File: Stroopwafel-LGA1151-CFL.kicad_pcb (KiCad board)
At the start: 2 copper layers, 2 parts

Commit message: replaced PCH symbol set with modified more sane version
seriously what was intel thinking when laying out half of those symbols, i can't make sense of their choices
if you want the original version take it from the commit before this one I guess
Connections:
- UPCH1 pad AA45: unconnected-(UPCH1-GPP_K15/GSXSRESET#-PadAA45) -> (no net)
- UPCH1 pad AB47: unconnected-(UPCH1-GPP_H12/SML2ALERT#-PadAB47) -> (no net)
- UPCH1 pad AC47: unconnected-(UPCH1-GPP_H15/SML3ALERT#-PadAC47) -> (no net)
- UPCH1 pad AD47: unconnected-(UPCH1-GPP_H11/SML2DATA-PadAD47) -> (no net)
- UPCH1 pad AD48: unconnected-(UPCH1-GPP_H14/SML3DATA-PadAD48) -> (no net)
- UPCH1 pad AE43: unconnected-(UPCH1-GPP_H16/SML4CLK-PadAE43) -> (no net)
- UPCH1 pad AE44: unconnected-(UPCH1-GPP_H18/SML4ALERT#-PadAE44) -> (no net)
- UPCH1 pad AE48: unconnected-(UPCH1-GPP_H10/SML2CLK-PadAE48) -> (no net)
- UPCH1 pad AF47: unconnected-(UPCH1-GPP_H13/SML3CLK-PadAF47) -> (no net)
- UPCH1 pad AJ46: unconnected-(UPCH1-GPP_H17/SML4DATA-PadAJ46) -> (no net)
- UPCH1 pad AL47: unconnected-(UPCH1-GPP_E3/CPU_GP0-PadAL47) -> (no net)
- UPCH1 pad AM45: unconnected-(UPCH1-GPP_E7/CPU_GP1-PadAM45) -> (no net)
- UPCH1 pad AT40: unconnected-(UPCH1-SPI0_CS2#-PadAT40) -> (no net)
- UPCH1 pad AU41: unconnected-(UPCH1-SPI0_MOSI-PadAU41) -> (no net)
- UPCH1 pad AV29: unconnected-(UPCH1-GPP_B13/PLTRST#-PadAV29) -> (no net)
- UPCH1 pad AW47: unconnected-(UPCH1-SPI0_CLK-PadAW47) -> (no net)
- UPCH1 pad AW48: unconnected-(UPCH1-SPI0_CS1#-PadAW48) -> (no net)
- UPCH1 pad AY47: unconnected-(UPCH1-SPI0_CS0#-PadAY47) -> (no net)
- UPCH1 pad AY48: unconnected-(UPCH1-SPI0_IO2-PadAY48) -> (no net)
- UPCH1 pad BA45: unconnected-(UPCH1-SPI0_MISO-PadBA45) -> (no net)
- UPCH1 pad BA46: unconnected-(UPCH1-SPI0_IO3-PadBA46) -> (no net)
- UPCH1 pad BB44: unconnected-(UPCH1-INTRUDER#-PadBB44) -> (no net)
- UPCH1 pad BC17: unconnected-(UPCH1-GPP_D22/SPI1_IO3-PadBC17) -> (no net)
- UPCH1 pad BC33: unconnected-(UPCH1-GPP_B4/CPU_GP3-PadBC33) -> (no net)
- UPCH1 pad BD17: unconnected-(UPCH1-GPP_D21/SPI1_IO2-PadBD17) -> (no net)
- UPCH1 pad BE18: unconnected-(UPCH1-GPP_D2/SPI1_MISO/SBK2/BK2-PadBE18) -> (no net)
- UPCH1 pad BE19: unconnected-(UPCH1-GPP_D1/SPI1_CLK/SBK1/BK1-PadBE19) -> (no net)
- UPCH1 pad BE36: unconnected-(UPCH1-GPP_A11/PME#/SD_VDD2_PWR_EN#-PadBE36) -> (no net)
- UPCH1 pad BF18: unconnected-(UPCH1-GPP_D3/SPI1_MOSI/SBK3/BK3-PadBF18) -> (no net)
- UPCH1 pad BF19: unconnected-(UPCH1-GPP_D0/SPI1_CS#/SBK0/BK0-PadBF19) -> (no net)
- UPCH1 pad BF32: unconnected-(UPCH1-GPP_B3/CPU_GP2-PadBF32) -> (no net)
- UPCH1 pad R13: unconnected-(UPCH1-RSVD1-PadR13) -> (no net)
- UPCH1 pad R15: unconnected-(UPCH1-RSVD2-PadR15) -> (no net)
- UPCH1 pad W46: unconnected-(UPCH1-GPP_K14/GSXDIN-PadW46) -> (no net)
- UPCH1 pad Y46: unconnected-(UPCH1-GPP_K12/GSXDOUT-PadY46) -> (no net)
- UPCH1 pad Y47: unconnected-(UPCH1-GPP_K16/GSXCLK-PadY47) -> (no net)
- UPCH1 pad Y48: unconnected-(UPCH1-GPP_K13/GSXSLOAD-PadY48) -> (no net)

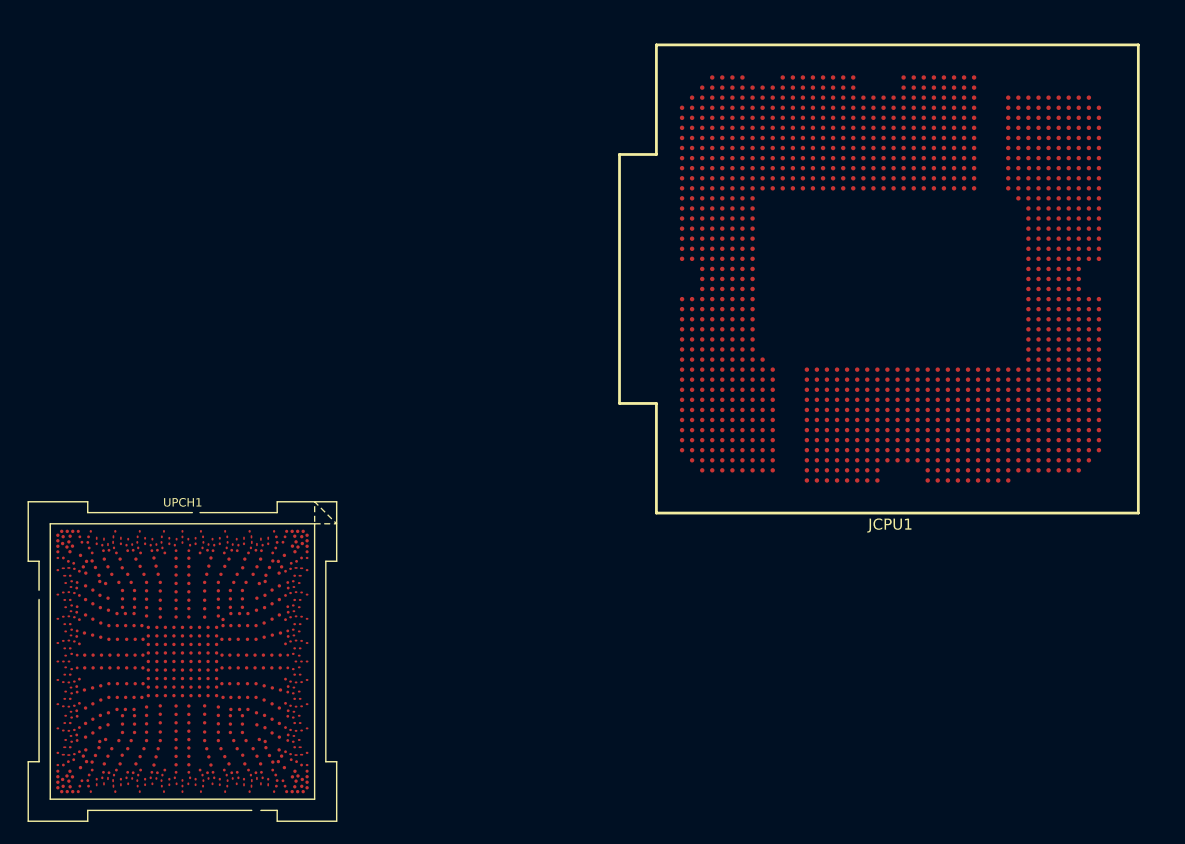
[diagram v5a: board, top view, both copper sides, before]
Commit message: Connected DMI for fun (with lane reversal)
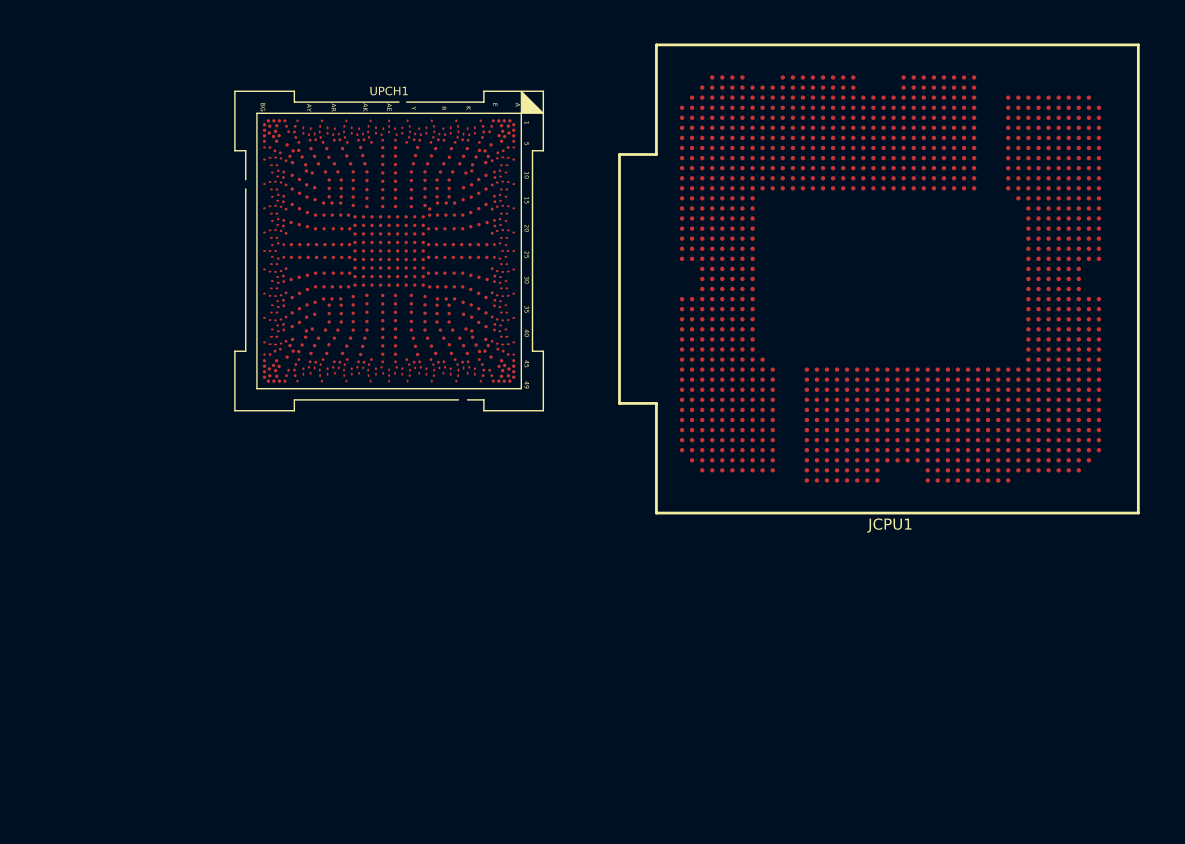
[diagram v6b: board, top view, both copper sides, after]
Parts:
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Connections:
- JCPU1 pad AA4: unconnected-(JCPU1C-DMI_RXP_1-PadAA4) -> DMI_CRx_PTx_1+
- JCPU1 pad AA5: unconnected-(JCPU1C-DMI_RXN_1-PadAA5) -> DMI_CRx_PTx_1-
- JCPU1 pad AB3: unconnected-(JCPU1C-DMI_RXN_2-PadAB3) -> DMI_CRx_PTx_2-
- JCPU1 pad AB4: unconnected-(JCPU1C-DMI_RXP_2-PadAB4) -> DMI_CRx_PTx_2+
- JCPU1 pad AC1: unconnected-(JCPU1C-DMI_TXN_0-PadAC1) -> DMI_CTx_PRx_0-
- JCPU1 pad AC2: unconnected-(JCPU1C-DMI_TXP_0-PadAC2) -> DMI_CTx_PRx_0+
- JCPU1 pad AC4: unconnected-(JCPU1C-DMI_RXP_3-PadAC4) -> DMI_CRx_PTx_3+
- JCPU1 pad AC5: unconnected-(JCPU1C-DMI_RXN_3-PadAC5) -> DMI_CRx_PTx_3-
- JCPU1 pad AD2: unconnected-(JCPU1C-DMI_TXN_1-PadAD2) -> DMI_CTx_PRx_1-
- JCPU1 pad AD3: unconnected-(JCPU1C-DMI_TXP_1-PadAD3) -> DMI_CTx_PRx_1+
- JCPU1 pad AE1: unconnected-(JCPU1C-DMI_TXN_2-PadAE1) -> DMI_CTx_PRx_2-
- JCPU1 pad AE2: unconnected-(JCPU1C-DMI_TXP_2-PadAE2) -> DMI_CTx_PRx_2+
- JCPU1 pad AF2: unconnected-(JCPU1C-DMI_TXP_3-PadAF2) -> DMI_CTx_PRx_3+
- JCPU1 pad AF3: unconnected-(JCPU1C-DMI_TXN_3-PadAF3) -> DMI_CTx_PRx_3-
- JCPU1 pad J5: (no net) -> unconnected-(JCPU1C-PEG_RXP_7-PadJ5)
- JCPU1 pad Y3: unconnected-(JCPU1C-DMI_RXP_0-PadY3) -> DMI_CRx_PTx_0+
- JCPU1 pad Y4: unconnected-(JCPU1C-DMI_RXN_0-PadY4) -> DMI_CRx_PTx_0-
- UPCH1 pad A13: (no net) -> unconnected-(UPCH1M-PCIE_RCOMPP-PadA13)
- UPCH1 pad A17: (no net) -> unconnected-(UPCH1B-PCIE1_TXN/USB3.1G1_7_TXN-PadA17)
- UPCH1 pad A2: (no net) -> GND
- UPCH1 pad A22: (no net) -> unconnected-(UPCH1B-PCIE5_TXP-PadA22)
- UPCH1 pad A25: (no net) -> unconnected-(UPCH1B-DMI7_TXP-PadA25)
- UPCH1 pad A28: (no net) -> GND
- UPCH1 pad A3: (no net) -> GND
- UPCH1 pad A33: (no net) -> GND
- UPCH1 pad A37: (no net) -> GND
- UPCH1 pad A4: (no net) -> GND
- UPCH1 pad A42: (no net) -> unconnected-(UPCH1C-PCIE17_TXN/SATA4_TXN-PadA42)
- UPCH1 pad A44: (no net) -> unconnected-(UPCH1C-PCIE20_TXN/SATA7_TXN-PadA44)
- UPCH1 pad A45: (no net) -> GND
- UPCH1 pad A46: (no net) -> GND
- UPCH1 pad A47: (no net) -> GND
- UPCH1 pad A48: (no net) -> GND
- UPCH1 pad A5: (no net) -> GND
- UPCH1 pad A6: (no net) -> unconnected-(UPCH1G-CLKOUT_CPUPCIBCLK_P-PadA6)
- UPCH1 pad A8: (no net) -> GND
- UPCH1 pad AA1: (no net) -> unconnected-(UPCH1G-CLKOUT_PCIE_N13-PadAA1)
- UPCH1 pad AA19: (no net) -> GND
- UPCH1 pad AA20: (no net) -> GND
- UPCH1 pad AA22: (no net) -> unconnected-(UPCH1H-VCCPRIM_1P05-PadAA22)
- UPCH1 pad AA23: (no net) -> unconnected-(UPCH1H-VCCPRIM_1P05-PadAA23)
- UPCH1 pad AA25: (no net) -> GND
- UPCH1 pad AA27: (no net) -> GND
- UPCH1 pad AA28: (no net) -> GND
- UPCH1 pad AA30: (no net) -> GND
- UPCH1 pad AA31: (no net) -> GND
- UPCH1 pad AA45: (no net) -> unconnected-(UPCH1A-GPP_K15/GSXSRESET#-PadAA45)
- UPCH1 pad AA49: (no net) -> GND
- UPCH1 pad AA5: (no net) -> GND
- UPCH1 pad AB19: (no net) -> GND
- UPCH1 pad AB2: (no net) -> unconnected-(UPCH1G-CLKOUT_PCIE_N5-PadAB2)
- UPCH1 pad AB20: (no net) -> unconnected-(UPCH1H-VCCPRIM_1P05-PadAB20)
- UPCH1 pad AB22: (no net) -> unconnected-(UPCH1H-VCCPRIM_1P05-PadAB22)
- UPCH1 pad AB23: (no net) -> unconnected-(UPCH1H-VCCPRIM_1P05-PadAB23)
- UPCH1 pad AB25: (no net) -> GND
- UPCH1 pad AB27: (no net) -> unconnected-(UPCH1H-VCCPRIM_1P05-PadAB27)
- UPCH1 pad AB28: (no net) -> unconnected-(UPCH1H-VCCPRIM_1P05-PadAB28)
- UPCH1 pad AB3: (no net) -> unconnected-(UPCH1G-CLKOUT_PCIE_P5-PadAB3)
- UPCH1 pad AB30: (no net) -> unconnected-(UPCH1H-VCCPRIM_1P05-PadAB30)
- UPCH1 pad AB31: (no net) -> GND
- UPCH1 pad AB47: (no net) -> unconnected-(UPCH1A-GPP_H12/SML2ALERT#-PadAB47)
- UPCH1 pad AB48: (no net) -> unconnected-(UPCH1G-GPP_H7/SRCCLKREQ13#-PadAB48)
- UPCH1 pad AC11: (no net) -> unconnected-(UPCH1G-CLKOUT_PCIE_P10-PadAC11)
- UPCH1 pad AC12: (no net) -> GND
- UPCH1 pad AC14: (no net) -> unconnected-(UPCH1G-CLKOUT_PCIE_N8-PadAC14)
- UPCH1 pad AC15: (no net) -> unconnected-(UPCH1G-CLKOUT_PCIE_P8-PadAC15)
- UPCH1 pad AC17: (no net) -> GND
- UPCH1 pad AC2: (no net) -> unconnected-(UPCH1G-CLKOUT_PCIE_N4-PadAC2)
- UPCH1 pad AC3: (no net) -> unconnected-(UPCH1G-CLKOUT_PCIE_P4-PadAC3)
- UPCH1 pad AC33: (no net) -> GND
- UPCH1 pad AC35: (no net) -> unconnected-(UPCH1H-VCCPGPPHK-PadAC35)
- UPCH1 pad AC36: (no net) -> unconnected-(UPCH1H-VCCPGPPHK-PadAC36)
- UPCH1 pad AC38: (no net) -> GND
- UPCH1 pad AC39: (no net) -> unconnected-(UPCH1G-GPP_H5/SRCCLKREQ11#-PadAC39)
- UPCH1 pad AC4: (no net) -> GND
- UPCH1 pad AC41: (no net) -> unconnected-(UPCH1G-GPP_H4/SRCCLKREQ10#-PadAC41)
- UPCH1 pad AC43: (no net) -> unconnected-(UPCH1G-GPP_H9/SRCCLKREQ15#-PadAC43)
- UPCH1 pad AC44: (no net) -> unconnected-(UPCH1G-GPP_H8/SRCCLKREQ14#-PadAC44)
- UPCH1 pad AC46: (no net) -> GND
- UPCH1 pad AC47: (no net) -> unconnected-(UPCH1A-GPP_H15/SML3ALERT#-PadAC47)
- UPCH1 pad AC48: (no net) -> unconnected-(UPCH1G-GPP_H1/SRCCLKREQ7#-PadAC48)
- UPCH1 pad AC6: (no net) -> unconnected-(UPCH1G-CLKOUT_PCIE_P12-PadAC6)
- UPCH1 pad AC7: (no net) -> unconnected-(UPCH1G-CLKOUT_PCIE_N12-PadAC7)
- UPCH1 pad AC9: (no net) -> unconnected-(UPCH1G-CLKOUT_PCIE_N10-PadAC9)
- UPCH1 pad AD1: (no net) -> GND
- UPCH1 pad AD19: (no net) -> GND
- UPCH1 pad AD2: (no net) -> GND
- UPCH1 pad AD20: (no net) -> unconnected-(UPCH1H-VCCPRIM_1P05-PadAD20)
- UPCH1 pad AD22: (no net) -> GND
- UPCH1 pad AD23: (no net) -> unconnected-(UPCH1H-VCCPRIM_1P05-PadAD23)
- UPCH1 pad AD25: (no net) -> GND
- UPCH1 pad AD27: (no net) -> unconnected-(UPCH1H-VCCPRIM_1P05-PadAD27)
- UPCH1 pad AD28: (no net) -> unconnected-(UPCH1H-VCCPRIM_1P05-PadAD28)
- UPCH1 pad AD3: (no net) -> unconnected-(UPCH1C-THRMTRIP#-PadAD3)
- UPCH1 pad AD30: (no net) -> unconnected-(UPCH1H-VCCPRIM_1P05-PadAD30)
- UPCH1 pad AD31: (no net) -> unconnected-(UPCH1H-VCCPRIM_1P05-PadAD31)
- UPCH1 pad AD47: (no net) -> unconnected-(UPCH1A-GPP_H11/SML2DATA-PadAD47)
- UPCH1 pad AD48: (no net) -> unconnected-(UPCH1A-GPP_H14/SML3DATA-PadAD48)
- UPCH1 pad AD49: (no net) -> GND
- UPCH1 pad AE11: (no net) -> unconnected-(UPCH1G-CLKOUT_PCIE_P11-PadAE11)
- UPCH1 pad AE12: (no net) -> GND
- UPCH1 pad AE14: (no net) -> unconnected-(UPCH1G-CLKOUT_PCIE_N2-PadAE14)
- UPCH1 pad AE15: (no net) -> unconnected-(UPCH1G-CLKOUT_PCIE_P2-PadAE15)
- UPCH1 pad AE17: (no net) -> unconnected-(UPCH1H-VCCPRIM_1P05-PadAE17)
- UPCH1 pad AE2: (no net) -> unconnected-(UPCH1C-PM_DOWN-PadAE2)
- UPCH1 pad AE3: (no net) -> unconnected-(UPCH1D-CPUPWRGD-PadAE3)
- UPCH1 pad AE33: (no net) -> GND
- UPCH1 pad AE35: (no net) -> unconnected-(UPCH1H-VCCPGPPEF-PadAE35)
- UPCH1 pad AE36: (no net) -> unconnected-(UPCH1H-VCCPGPPEF-PadAE36)
- UPCH1 pad AE38: (no net) -> GND
- UPCH1 pad AE39: (no net) -> unconnected-(UPCH1G-GPP_H6/SRCCLKREQ12#-PadAE39)
- UPCH1 pad AE4: (no net) -> GND
- UPCH1 pad AE41: (no net) -> unconnected-(UPCH1G-GPP_H2/SRCCLKREQ8#-PadAE41)
- UPCH1 pad AE43: (no net) -> unconnected-(UPCH1A-GPP_H16/SML4CLK-PadAE43)
- UPCH1 pad AE44: (no net) -> unconnected-(UPCH1A-GPP_H18/SML4ALERT#-PadAE44)
- UPCH1 pad AE46: (no net) -> GND
- UPCH1 pad AE47: (no net) -> unconnected-(UPCH1G-GPP_H0/SRCCLKREQ6#-PadAE47)
- UPCH1 pad AE48: (no net) -> unconnected-(UPCH1A-GPP_H10/SML2CLK-PadAE48)
- UPCH1 pad AE6: (no net) -> unconnected-(UPCH1G-CLKOUT_PCIE_N3-PadAE6)
- UPCH1 pad AE7: (no net) -> unconnected-(UPCH1G-CLKOUT_PCIE_P3-PadAE7)
- UPCH1 pad AE9: (no net) -> unconnected-(UPCH1G-CLKOUT_PCIE_N11-PadAE9)
- UPCH1 pad AF19: (no net) -> unconnected-(UPCH1H-VCCPRIM_1P8-PadAF19)
- UPCH1 pad AF2: (no net) -> unconnected-(UPCH1C-PECI-PadAF2)
- UPCH1 pad AF20: (no net) -> unconnected-(UPCH1H-VCCPRIM_1P8-PadAF20)
- UPCH1 pad AF22: (no net) -> GND
- UPCH1 pad AF23: (no net) -> unconnected-(UPCH1H-VCCPRIM_1P05-PadAF23)
- UPCH1 pad AF25: (no net) -> GND
- UPCH1 pad AF27: (no net) -> unconnected-(UPCH1H-VCCPRIM_1P05-PadAF27)
- UPCH1 pad AF28: (no net) -> GND
- UPCH1 pad AF3: (no net) -> unconnected-(UPCH1C-PM_SYNC-PadAF3)
- UPCH1 pad AF30: (no net) -> unconnected-(UPCH1H-VCCPRIM_1P05-PadAF30)
- UPCH1 pad AF31: (no net) -> unconnected-(UPCH1H-VCCPRIM_1P05-PadAF31)
- UPCH1 pad AF47: (no net) -> unconnected-(UPCH1A-GPP_H13/SML3CLK-PadAF47)
- UPCH1 pad AF48: (no net) -> unconnected-(UPCH1G-GPP_H3/SRCCLKREQ9#-PadAF48)
- UPCH1 pad AG1: (no net) -> GND
- UPCH1 pad AG19: (no net) -> unconnected-(UPCH1H-VCCPRIM_1P8-PadAG19)
- UPCH1 pad AG20: (no net) -> unconnected-(UPCH1H-VCCPRIM_1P8-PadAG20)
- UPCH1 pad AG22: (no net) -> GND
- UPCH1 pad AG23: (no net) -> GND
- UPCH1 pad AG25: (no net) -> GND
- UPCH1 pad AG27: (no net) -> GND
- UPCH1 pad AG28: (no net) -> GND
- UPCH1 pad AG30: (no net) -> GND
- UPCH1 pad AG31: (no net) -> unconnected-(UPCH1H-VCCPRIM_1P05-PadAG31)
- UPCH1 pad AG45: (no net) -> unconnected-(UPCH1K-GPP_H20/ISH_I2C0_SCL-PadAG45)
- UPCH1 pad AG49: (no net) -> GND
- UPCH1 pad AG5: (no net) -> unconnected-(UPCH1C-PLTRST_CPU#-PadAG5)
- UPCH1 pad AH10: (no net) -> unconnected-(UPCH1G-CLKOUT_PCIE_P1-PadAH10)
- UPCH1 pad AH12: (no net) -> GND
- UPCH1 pad AH14: (no net) -> unconnected-(UPCH1J-RSVD12-PadAH14)
- UPCH1 pad AH15: (no net) -> unconnected-(UPCH1J-RSVD13-PadAH15)
- UPCH1 pad AH17: (no net) -> GND
- UPCH1 pad AH2: (no net) -> unconnected-(UPCH1D-PCH_JTAG_TDI-PadAH2)
- UPCH1 pad AH3: (no net) -> unconnected-(UPCH1D-PCH_JTAG_TDO-PadAH3)
- UPCH1 pad AH33: (no net) -> GND
- UPCH1 pad AH35: (no net) -> unconnected-(UPCH1F-GPP_E5/SATA_DEVSLP1-PadAH35)
- UPCH1 pad AH36: (no net) -> unconnected-(UPCH1B-GPP_E9/USB2_OC0#-PadAH36)
- UPCH1 pad AH38: (no net) -> GND
- UPCH1 pad AH4: (no net) -> unconnected-(UPCH1D-PCH_JTAGX-PadAH4)
- UPCH1 pad AH40: (no net) -> unconnected-(UPCH1F-GPP_E6/SATA_DEVSLP2-PadAH40)
- UPCH1 pad AH41: (no net) -> unconnected-(UPCH1C-GPP_E0/SATAxPCIE0/SATAGP0-PadAH41)
- UPCH1 pad AH46: (no net) -> unconnected-(UPCH1K-GPP_H19/ISH_I2C0_SDA-PadAH46)
- UPCH1 pad AH47: (no net) -> unconnected-(UPCH1K-GPP_H22/ISH_I2C1_SCL-PadAH47)
- UPCH1 pad AH48: (no net) -> unconnected-(UPCH1K-GPP_H21/ISH_I2C1_SDA-PadAH48)
- UPCH1 pad AH9: (no net) -> unconnected-(UPCH1G-CLKOUT_PCIE_N1-PadAH9)
- UPCH1 pad AJ19: (no net) -> GND
- UPCH1 pad AJ20: (no net) -> GND
- UPCH1 pad AJ22: (no net) -> unconnected-(UPCH1H-VCCDPHY_1P24-PadAJ22)
- UPCH1 pad AJ23: (no net) -> unconnected-(UPCH1H-VCCDPHY_1P24-PadAJ23)
- UPCH1 pad AJ25: (no net) -> GND
- UPCH1 pad AJ27: (no net) -> GND
- UPCH1 pad AJ28: (no net) -> GND
- UPCH1 pad AJ3: (no net) -> unconnected-(UPCH1D-PCH_JTAG_TCK-PadAJ3)
- UPCH1 pad AJ30: (no net) -> GND
- UPCH1 pad AJ31: (no net) -> GND
- UPCH1 pad AJ4: (no net) -> unconnected-(UPCH1D-PCH_JTAG_TMS-PadAJ4)
- UPCH1 pad AJ43: (no net) -> unconnected-(UPCH1C-GPP_E1/SATAxPCIE1/SATAGP1-PadAJ43)
- UPCH1 pad AJ44: (no net) -> unconnected-(UPCH1B-GPP_E11/USB2_OC2#-PadAJ44)
- UPCH1 pad AJ46: (no net) -> unconnected-(UPCH1A-GPP_H17/SML4DATA-PadAJ46)
- UPCH1 pad AJ47: (no net) -> unconnected-(UPCH1E-GPP_H23/TIME_SYNC0-PadAJ47)
- UPCH1 pad AJ6: (no net) -> unconnected-(UPCH1G-CLKOUT_PCIE_N0-PadAJ6)
- UPCH1 pad AJ7: (no net) -> unconnected-(UPCH1G-CLKOUT_PCIE_P0-PadAJ7)
- UPCH1 pad AK19: (no net) -> GND
- UPCH1 pad AK2: (no net) -> unconnected-(UPCH1J-TRIGGER_IN-PadAK2)
- UPCH1 pad AK20: (no net) -> GND
- UPCH1 pad AK22: (no net) -> unconnected-(UPCH1H-VCCPRIM_1P24-PadAK22)
- UPCH1 pad AK23: (no net) -> unconnected-(UPCH1H-VCCPRIM_1P24-PadAK23)
- UPCH1 pad AK25: (no net) -> GND
- UPCH1 pad AK27: (no net) -> GND
- UPCH1 pad AK28: (no net) -> GND
- UPCH1 pad AK3: (no net) -> unconnected-(UPCH1J-TRIGGER_OUT-PadAK3)
- UPCH1 pad AK30: (no net) -> GND
- UPCH1 pad AK31: (no net) -> GND
- UPCH1 pad AK4: (no net) -> GND
- UPCH1 pad AK46: (no net) -> GND
- UPCH1 pad AK47: (no net) -> unconnected-(UPCH1C-GPP_E2/SATAxPCIE2/SATAGP2-PadAK47)
- UPCH1 pad AK48: (no net) -> unconnected-(UPCH1C-GPP_E8/SATALED#-PadAK48)
- UPCH1 pad AL10: (no net) -> unconnected-(UPCH1E-GPP_I8/DDPC_CTRLDATA-PadAL10)
- UPCH1 pad AL12: (no net) -> GND
- UPCH1 pad AL13: (no net) -> unconnected-(UPCH1E-GPP_I5/DDPB_CTRLCLK-PadAL13)
- UPCH1 pad AL15: (no net) -> unconnected-(UPCH1E-GPP_I3/DDPE_HPD3/DISP_MISC3-PadAL15)
- UPCH1 pad AL17: (no net) -> GND
- UPCH1 pad AL2: (no net) -> unconnected-(UPCH1J-PREQ#-PadAL2)
- UPCH1 pad AL21: (no net) -> GND
- UPCH1 pad AL24: (no net) -> GND
- UPCH1 pad AL26: (no net) -> GND
- UPCH1 pad AL29: (no net) -> GND
- UPCH1 pad AL3: (no net) -> unconnected-(UPCH1D-ITP_PMODE-PadAL3)
- UPCH1 pad AL33: (no net) -> GND
- UPCH1 pad AL35: (no net) -> unconnected-(UPCH1M-TP2-PadAL35)
- UPCH1 pad AL37: (no net) -> unconnected-(UPCH1A-VSS-PadAL37)
- UPCH1 pad AL38: (no net) -> GND
- UPCH1 pad AL40: (no net) -> unconnected-(UPCH1B-GPP_E10/USB2_OC1#-PadAL40)
- UPCH1 pad AL41: (no net) -> unconnected-(UPCH1B-GPP_E12/USB2_OC3#-PadAL41)
- UPCH1 pad AL47: (no net) -> unconnected-(UPCH1A-GPP_E3/CPU_GP0-PadAL47)
- UPCH1 pad AL48: (no net) -> unconnected-(UPCH1F-GPP_E4/SATA_DEVSLP0-PadAL48)
- UPCH1 pad AL9: (no net) -> unconnected-(UPCH1E-GPP_I9/DDPD_CTRLCLK-PadAL9)
- UPCH1 pad AM1: (no net) -> GND
- UPCH1 pad AM18: (no net) -> GND
- UPCH1 pad AM2: (no net) -> unconnected-(UPCH1D-HDACPU_SDO-PadAM2)
- UPCH1 pad AM3: (no net) -> unconnected-(UPCH1D-HDACPU_SCLK-PadAM3)
- UPCH1 pad AM32: (no net) -> GND
- UPCH1 pad AM4: (no net) -> unconnected-(UPCH1J-CPU_TRST#-PadAM4)
- UPCH1 pad AM43: (no net) -> unconnected-(UPCH1C-GPP_F2/SATAxPCIE5/SATAGP5-PadAM43)
- UPCH1 pad AM45: (no net) -> unconnected-(UPCH1A-GPP_E7/CPU_GP1-PadAM45)
- UPCH1 pad AM46: (no net) -> unconnected-(UPCH1C-GPP_F1/SATAxPCIE4/SATAGP4-PadAM46)
- UPCH1 pad AM47: (no net) -> unconnected-(UPCH1C-GPP_F3/SATAxPCIE6/SATAGP6-PadAM47)
- UPCH1 pad AM48: (no net) -> unconnected-(UPCH1C-GPP_F4/SATAxPCIE7/SATAGP7-PadAM48)
- UPCH1 pad AM49: (no net) -> GND
- UPCH1 pad AM5: (no net) -> unconnected-(UPCH1J-PRDY#-PadAM5)
- UPCH1 pad AM7: (no net) -> unconnected-(UPCH1M-GPP_I14/M2_SKT2_CFG3-PadAM7)
- UPCH1 pad AN10: (no net) -> unconnected-(UPCH1E-GPP_I1/DDPC_HPD1/DISP_MISC1-PadAN10)
- UPCH1 pad AN12: (no net) -> GND
- UPCH1 pad AN13: (no net) -> unconnected-(UPCH1E-GPP_I7/DDPC_CTRLCLK-PadAN13)
- UPCH1 pad AN15: (no net) -> unconnected-(UPCH1H-VCCPRIM_1P8-PadAN15)
- UPCH1 pad AN16: (no net) -> GND
- UPCH1 pad AN18: (no net) -> unconnected-(UPCH1K-GPP_D12/ISH_SPI_MOSI/GP_BSSB_DI/GSPI2_MOSI-PadAN18)
- UPCH1 pad AN21: (no net) -> unconnected-(UPCH1H-VCCPGPPG_3P3-PadAN21)
- UPCH1 pad AN24: (no net) -> unconnected-(UPCH1H-VCCPGPPD-PadAN24)
- UPCH1 pad AN26: (no net) -> unconnected-(UPCH1H-VCCPGPPBC-PadAN26)
- UPCH1 pad AN29: (no net) -> unconnected-(UPCH1G-GPP_B10/SRCCLKREQ5#-PadAN29)
- UPCH1 pad AN3: (no net) -> unconnected-(UPCH1D-HDACPU_SDI-PadAN3)
- UPCH1 pad AN32: (no net) -> unconnected-(UPCH1H-VCCPGPPA-PadAN32)
- UPCH1 pad AN34: (no net) -> GND
- UPCH1 pad AN35: (no net) -> unconnected-(UPCH1A-TP1-PadAN35)
- UPCH1 pad AN37: (no net) -> unconnected-(UPCH1F-GPP_F8/SATA_DEVSLP6-PadAN37)
- UPCH1 pad AN38: (no net) -> GND
- UPCH1 pad AN4: (no net) -> unconnected-(UPCH1M-GPP_I13/M2_SKT2_CFG2-PadAN4)
- UPCH1 pad AN40: (no net) -> unconnected-(UPCH1E-GPP_F23/DDPF_CTRLDATA-PadAN40)
- UPCH1 pad AN44: (no net) -> unconnected-(UPCH1H-VCCSPI-PadAN44)
- UPCH1 pad AN46: (no net) -> unconnected-(UPCH1F-GPP_F7/SATA_DEVSLP5-PadAN46)
- UPCH1 pad AN47: (no net) -> unconnected-(UPCH1C-GPP_F0/SATAxPCIE3/SATAGP3-PadAN47)
- UPCH1 pad AN6: (no net) -> unconnected-(UPCH1E-GPP_I4/EDP_HPD/DISP_MISC4-PadAN6)
- UPCH1 pad AP2: (no net) -> unconnected-(UPCH1M-GPP_I12/M2_SKT2_CFG1-PadAP2)
- UPCH1 pad AP21: (no net) -> unconnected-(UPCH1K-GPP_C13/UART1_TXD/ISH_UART1_TXD-PadAP21)
- UPCH1 pad AP24: (no net) -> unconnected-(UPCH1K-GPP_C11/UART0_CTS#-PadAP24)
- UPCH1 pad AP26: (no net) -> unconnected-(UPCH1H-VCCPGPPBC-PadAP26)
- UPCH1 pad AP29: (no net) -> unconnected-(UPCH1D-GPP_B11/I2S_MCLK-PadAP29)
- UPCH1 pad AP3: (no net) -> unconnected-(UPCH1M-GPP_I11/M2_SKT2_CFG0-PadAP3)
- UPCH1 pad AP4: (no net) -> GND
- UPCH1 pad AP41: (no net) -> unconnected-(UPCH1E-GPP_F14/PS_ON#-PadAP41)
- UPCH1 pad AP46: (no net) -> GND
- UPCH1 pad AP47: (no net) -> unconnected-(UPCH1F-GPP_F9/SATA_DEVSLP7-PadAP47)
- UPCH1 pad AP48: (no net) -> unconnected-(UPCH1F-GPP_F5/SATA_DEVSLP3-PadAP48)
- UPCH1 pad AP9: (no net) -> unconnected-(UPCH1E-GPP_I2/DDPD_HPD2/DISP_MISC2-PadAP9)
- UPCH1 pad AR12: (no net) -> GND
- UPCH1 pad AR13: (no net) -> unconnected-(UPCH1M-GPP_J11/A4WP_PRESENT-PadAR13)
- UPCH1 pad AR15: (no net) -> unconnected-(UPCH1H-VCCPRIM_1P8-PadAR15)
- UPCH1 pad AR16: (no net) -> GND
- UPCH1 pad AR18: (no net) -> unconnected-(UPCH1K-GPP_D15/ISH_UART0_RTS#/GSPI2_CS1#/CNV_WFEN-PadAR18)
- UPCH1 pad AR2: (no net) -> unconnected-(UPCH1C-CL_CLK-PadAR2)
- UPCH1 pad AR3: (no net) -> unconnected-(UPCH1E-GPP_I10/DDPD_CTRLDATA-PadAR3)
- UPCH1 pad AR32: (no net) -> unconnected-(UPCH1G-GPP_B7/SRCCLKREQ2#-PadAR32)
- UPCH1 pad AR34: (no net) -> GND
- UPCH1 pad AR35: (no net) -> unconnected-(UPCH1B-GPP_E16/USB2_OC5#-PadAR35)
- UPCH1 pad AR37: (no net) -> unconnected-(UPCH1B-GPP_E17/USB2_OC6#-PadAR37)
- UPCH1 pad AR38: (no net) -> GND
- UPCH1 pad AR42: (no net) -> unconnected-(UPCH1C-GPP_F10/SATA_SCLOCK-PadAR42)
- UPCH1 pad AR47: (no net) -> unconnected-(UPCH1F-GPP_F6/SATA_DEVSLP4-PadAR47)
- UPCH1 pad AR48: (no net) -> unconnected-(UPCH1C-GPP_F11/SATA_SLOAD-PadAR48)
- UPCH1 pad AR8: (no net) -> unconnected-(UPCH1E-GPP_I6/DDPB_CTRLDATA-PadAR8)
- UPCH1 pad AT1: (no net) -> GND
- UPCH1 pad AT10: (no net) -> unconnected-(UPCH1M-GPP_J3-PadAT10)
- UPCH1 pad AT16: (no net) -> GND
- UPCH1 pad AT18: (no net) -> GND
- UPCH1 pad AT21: (no net) -> GND
- UPCH1 pad AT24: (no net) -> GND
- UPCH1 pad AT26: (no net) -> GND
- UPCH1 pad AT29: (no net) -> GND
- UPCH1 pad AT32: (no net) -> GND
- UPCH1 pad AT34: (no net) -> GND
- UPCH1 pad AT40: (no net) -> unconnected-(UPCH1A-SPI0_CS2#-PadAT40)
- UPCH1 pad AT44: (no net) -> unconnected-(UPCH1H-VCCPRIM_3P3-PadAT44)
- UPCH1 pad AT45: (no net) -> GND
- UPCH1 pad AT49: (no net) -> unconnected-(UPCH1E-GPP_F22/DDPF_CTRLCLK-PadAT49)
- UPCH1 pad AT5: (no net) -> unconnected-(UPCH1C-CL_DATA-PadAT5)
- UPCH1 pad AT6: (no net) -> unconnected-(UPCH1E-GPP_I0/DDPB_HPD0/DISP_MISC0-PadAT6)
- UPCH1 pad AU2: (no net) -> unconnected-(UPCH1D-SYS_RESET#-PadAU2)
- UPCH1 pad AU24: (no net) -> unconnected-(UPCH1K-GPP_C12/UART1_RXD/ISH_UART1_RXD-PadAU24)
- UPCH1 pad AU26: (no net) -> unconnected-(UPCH1K-GPP_B20/GSPI1_CLK-PadAU26)
- UPCH1 pad AU3: (no net) -> unconnected-(UPCH1D-SYS_PWROK-PadAU3)
- UPCH1 pad AU4: (no net) -> unconnected-(UPCH1C-CL_RST#-PadAU4)
- UPCH1 pad AU41: (no net) -> unconnected-(UPCH1A-SPI0_MOSI-PadAU41)
- UPCH1 pad AU46: (no net) -> unconnected-(UPCH1C-GPP_F12/SATA_SDATAOUT1-PadAU46)
- UPCH1 pad AU47: (no net) -> unconnected-(UPCH1C-GPP_F13/SATA_SDATAOUT0-PadAU47)
- UPCH1 pad AU48: (no net) -> unconnected-(UPCH1C-GPP_F21/EDP_BKLTCTL-PadAU48)
- UPCH1 pad AU9: (no net) -> unconnected-(UPCH1M-GPP_J9/CNV_MFUART2_TXD-PadAU9)
- UPCH1 pad AV11: (no net) -> GND
- UPCH1 pad AV13: (no net) -> unconnected-(UPCH1M-GPP_G7/SD_WP-PadAV13)
- UPCH1 pad AV16: (no net) -> unconnected-(UPCH1D-GPP_D18/DMIC_DATA1/SNDW3_DATA-PadAV16)
- UPCH1 pad AV18: (no net) -> unconnected-(UPCH1D-GPP_D8/I2S2_SCLK-PadAV18)
- UPCH1 pad AV21: (no net) -> unconnected-(UPCH1K-GPP_C23/UART2_CTS#-PadAV21)
- UPCH1 pad AV29: (no net) -> unconnected-(UPCH1A-GPP_B13/PLTRST#-PadAV29)
- UPCH1 pad AV3: (no net) -> unconnected-(UPCH1M-GPP_J7/CNV_RGI_RSP/UART0B_CTS#-PadAV3)
- UPCH1 pad AV32: (no net) -> unconnected-(UPCH1D-GPP_A8/CLKRUN#-PadAV32)
- UPCH1 pad AV34: (no net) -> unconnected-(UPCH1K-GPP_A23/ISH_GP5-PadAV34)
- UPCH1 pad AV37: (no net) -> unconnected-(UPCH1F-GPP_A3/LAD2/ESPI_IO2-PadAV37)
- UPCH1 pad AV39: (no net) -> GND
- UPCH1 pad AV4: (no net) -> unconnected-(UPCH1M-GPP_J4/CNV_BRI_DT/UART0B_RTS#-PadAV4)
- UPCH1 pad AV43: (no net) -> unconnected-(UPCH1B-GPP_E18/USB2_OC7#-PadAV43)
- UPCH1 pad AV44: (no net) -> unconnected-(UPCH1C-GPP_F19/EDP_VDDEN-PadAV44)
- UPCH1 pad AV46: (no net) -> unconnected-(UPCH1C-GPP_F20/EDP_BKLTEN-PadAV46)
- UPCH1 pad AV47: (no net) -> unconnected-(UPCH1B-GPP_E15/USB2_OC4#-PadAV47)
- UPCH1 pad AV6: (no net) -> unconnected-(UPCH1M-GPP_J0/CNV_PA_BLANKING-PadAV6)
- UPCH1 pad AV7: (no net) -> unconnected-(UPCH1M-GPP_J10-PadAV7)
- UPCH1 pad AW10: (no net) -> GND
- UPCH1 pad AW13: (no net) -> unconnected-(UPCH1M-GPP_G0/SD_CMD-PadAW13)
- UPCH1 pad AW15: (no net) -> unconnected-(UPCH1D-GPP_D17/DMIC_CLK1/SNDW3_CLK-PadAW15)
- UPCH1 pad AW18: (no net) -> unconnected-(UPCH1D-GPP_D7/I2S2_RXD-PadAW18)
- UPCH1 pad AW2: (no net) -> unconnected-(UPCH1M-GPP_J8/CNV_MFUART2_RXD-PadAW2)
- UPCH1 pad AW21: (no net) -> unconnected-(UPCH1K-GPP_C22/UART2_RTS#-PadAW21)
- UPCH1 pad AW24: (no net) -> unconnected-(UPCH1K-GPP_C14/UART1_RTS#/ISH_UART1_RTS#-PadAW24)
- UPCH1 pad AW26: (no net) -> unconnected-(UPCH1K-GPP_B19/GSPI1_CS0#-PadAW26)
- UPCH1 pad AW29: (no net) -> unconnected-(UPCH1D-GPP_B14/SPKR-PadAW29)
- UPCH1 pad AW3: (no net) -> unconnected-(UPCH1M-GPP_J2-PadAW3)
- UPCH1 pad AW32: (no net) -> unconnected-(UPCH1K-GPP_A22/ISH_GP4-PadAW32)
- UPCH1 pad AW35: (no net) -> unconnected-(UPCH1F-GPP_A6/SERIRQ/ESPI_CS1#-PadAW35)
- UPCH1 pad AW37: (no net) -> unconnected-(UPCH1F-GPP_A2/LAD1/ESPI_IO1-PadAW37)
- UPCH1 pad AW4: (no net) -> GND
- UPCH1 pad AW40: (no net) -> GND
- UPCH1 pad AW41: (no net) -> unconnected-(UPCH1D-DSW_PWROK-PadAW41)
- UPCH1 pad AW46: (no net) -> GND
- UPCH1 pad AW47: (no net) -> unconnected-(UPCH1A-SPI0_CLK-PadAW47)
- UPCH1 pad AW48: (no net) -> unconnected-(UPCH1A-SPI0_CS1#-PadAW48)
- UPCH1 pad AW9: (no net) -> unconnected-(UPCH1H-VCCPRIM_3P3-PadAW9)
- UPCH1 pad AY2: (no net) -> unconnected-(UPCH1M-GPP_J5/CNV_BRI_RSP/UART0B_RXD-PadAY2)
- UPCH1 pad AY3: (no net) -> unconnected-(UPCH1M-GPP_J1/CPU_VCCIO_PWR_GATE#-PadAY3)
- UPCH1 pad AY42: (no net) -> unconnected-(UPCH1D-PCH_PWROK-PadAY42)
- UPCH1 pad AY47: (no net) -> unconnected-(UPCH1A-SPI0_CS0#-PadAY47)
- UPCH1 pad AY48: (no net) -> unconnected-(UPCH1A-SPI0_IO2-PadAY48)
- UPCH1 pad AY8: (no net) -> unconnected-(UPCH1H-VCCPRIM_3P3-PadAY8)
- UPCH1 pad B1: (no net) -> unconnected-(UPCH1H-VCCAPLL_1P05-PadB1)
- UPCH1 pad B10: (no net) -> unconnected-(UPCH1F-USB3.1G2_3_RXN-PadB10)
- UPCH1 pad B12: (no net) -> unconnected-(UPCH1M-PCIE_RCOMPN-PadB12)
- UPCH1 pad B14: (no net) -> unconnected-(UPCH1F-USB3.1G2_4_TXN-PadB14)
- UPCH1 pad B15: (no net) -> unconnected-(UPCH1F-USB3.1G2_5_TXP-PadB15)
- UPCH1 pad B17: (no net) -> unconnected-(UPCH1B-PCIE1_TXP/USB3.1G1_7_TXP-PadB17)
- UPCH1 pad B18: (no net) -> unconnected-(UPCH1B-PCIE2_TXN/USB3.1G1_8_TXN-PadB18)
- UPCH1 pad B19: (no net) -> unconnected-(UPCH1B-PCIE3_TXN/USB3.1G1_9_TXN-PadB19)
- UPCH1 pad B2: (no net) -> unconnected-(UPCH1H-VCCAPLL_1P05-PadB2)
- UPCH1 pad B21: (no net) -> unconnected-(UPCH1B-PCIE5_TXN-PadB21)
- UPCH1 pad B23: (no net) -> unconnected-(UPCH1B-PCIE7_TXP-PadB23)
- UPCH1 pad B24: (no net) -> unconnected-(UPCH1B-PCIE8_TXN-PadB24)
- UPCH1 pad B25: (no net) -> unconnected-(UPCH1B-DMI7_TXN-PadB25)
- UPCH1 pad B26: (no net) -> unconnected-(UPCH1B-DMI6_TXN-PadB26)
- UPCH1 pad B27: (no net) -> unconnected-(UPCH1B-DMI5_TXP-PadB27)
- UPCH1 pad B29: (no net) -> DMI_CRx_PTx_0+
- UPCH1 pad B3: (no net) -> unconnected-(UPCH1H-VCCAPLL_1P05-PadB3)
- UPCH1 pad B31: (no net) -> DMI_CRx_PTx_1+
- UPCH1 pad B32: (no net) -> DMI_CRx_PTx_2+
- UPCH1 pad B33: (no net) -> DMI_CRx_PTx_3+
- UPCH1 pad B35: (no net) -> unconnected-(UPCH1C-PCIE10_TXP-PadB35)
- UPCH1 pad B36: (no net) -> unconnected-(UPCH1C-PCIE11_TXN/SATA0A_TXN-PadB36)
- UPCH1 pad B38: (no net) -> unconnected-(UPCH1C-PCIE13_TXN/SATA0B_TXN-PadB38)
- UPCH1 pad B40: (no net) -> unconnected-(UPCH1C-PCIE15_TXN/SATA2_TXN-PadB40)
- UPCH1 pad B41: (no net) -> unconnected-(UPCH1C-PCIE16_TXN/SATA3_TXN-PadB41)
- UPCH1 pad B42: (no net) -> unconnected-(UPCH1C-PCIE17_TXP/SATA4_TXP-PadB42)
- UPCH1 pad B44: (no net) -> unconnected-(UPCH1C-PCIE20_TXP/SATA7_TXP-PadB44)
- UPCH1 pad B47: (no net) -> GND
- UPCH1 pad B48: (no net) -> GND
- UPCH1 pad B49: (no net) -> GND
- UPCH1 pad B6: (no net) -> unconnected-(UPCH1G-CLKOUT_CPUPCIBCLK_N-PadB6)
- UPCH1 pad B8: (no net) -> unconnected-(UPCH1G-CLKOUT_CPUBCLK_P-PadB8)
- UPCH1 pad B9: (no net) -> unconnected-(UPCH1F-USB3.1G2_2_RXN-PadB9)
- UPCH1 pad BA1: (no net) -> unconnected-(UPCH1M-CNV_WT_RCOMP-PadBA1)
- UPCH1 pad BA12: (no net) -> GND
- UPCH1 pad BA14: (no net) -> GND
- UPCH1 pad BA17: (no net) -> unconnected-(UPCH1D-GPP_D6/I2S2_TXD/MODEM_CLKREQ-PadBA17)
- UPCH1 pad BA2: (no net) -> unconnected-(UPCH1M-CNV_WR_D1P-PadBA2)
- UPCH1 pad BA20: (no net) -> unconnected-(UPCH1K-GPP_D9/ISH_SPI_CS#/GSPI2_CS0#-PadBA20)
- UPCH1 pad BA24: (no net) -> unconnected-(UPCH1K-GPP_C10/UART0_RTS#-PadBA24)
- UPCH1 pad BA26: (no net) -> unconnected-(UPCH1K-GPP_B22/GSPI1_MOSI-PadBA26)
- UPCH1 pad BA3: (no net) -> unconnected-(UPCH1M-CNV_WR_D1N-PadBA3)
- UPCH1 pad BA30: (no net) -> unconnected-(UPCH1G-GPP_B9/SRCCLKREQ4#-PadBA30)
- UPCH1 pad BA33: (no net) -> unconnected-(UPCH1K-GPP_A21/ISH_GP3-PadBA33)
- UPCH1 pad BA36: (no net) -> unconnected-(UPCH1F-GPP_A7/PIRQA#/ESPI_ALERT0#-PadBA36)
- UPCH1 pad BA38: (no net) -> unconnected-(UPCH1F-GPP_A4/LAD3/ESPI_IO3-PadBA38)
- UPCH1 pad BA4: (no net) -> unconnected-(UPCH1M-GPP_J6/CNV_RGI_DT/UART0B_TXD-PadBA4)
- UPCH1 pad BA44: (no net) -> GND
- UPCH1 pad BA45: (no net) -> unconnected-(UPCH1A-SPI0_MISO-PadBA45)
- UPCH1 pad BA46: (no net) -> unconnected-(UPCH1A-SPI0_IO3-PadBA46)
- UPCH1 pad BA47: (no net) -> unconnected-(UPCH1D-RSMRST#-PadBA47)
- UPCH1 pad BA48: (no net) -> unconnected-(UPCH1G-RTCX2-PadBA48)
- UPCH1 pad BA49: (no net) -> unconnected-(UPCH1G-RTCX1-PadBA49)
- UPCH1 pad BA5: (no net) -> GND
- UPCH1 pad BA6: (no net) -> GND
- UPCH1 pad BB11: (no net) -> unconnected-(UPCH1H-VCCPRIM_1P8-PadBB11)
- UPCH1 pad BB14: (no net) -> unconnected-(UPCH1H-VCCHDA-PadBB14)
- UPCH1 pad BB16: (no net) -> unconnected-(UPCH1K-GPP_D11/ISH_SPI_MISO/GP_BSSB_CLK/GSPI2_MISO-PadBB16)
- UPCH1 pad BB20: (no net) -> unconnected-(UPCH1K-GPP_D10/ISH_SPI_CLK/GSPI2_CLK-PadBB20)
- UPCH1 pad BB24: (no net) -> unconnected-(UPCH1K-GPP_C9/UART0_TXD-PadBB24)
- UPCH1 pad BB26: (no net) -> unconnected-(UPCH1K-GPP_B15/GSPI0_CS0#-PadBB26)
- UPCH1 pad BB3: (no net) -> unconnected-(UPCH1M-CNV_WR_D0N-PadBB3)
- UPCH1 pad BB30: (no net) -> unconnected-(UPCH1G-GPP_B8/SRCCLKREQ3#-PadBB30)
- UPCH1 pad BB34: (no net) -> unconnected-(UPCH1F-GPP_A10/CLKOUT_LPC1-PadBB34)
- UPCH1 pad BB36: (no net) -> unconnected-(UPCH1F-GPP_A9/CLKOUT_LPC0/ESPI_CLK-PadBB36)
- UPCH1 pad BB39: (no net) -> unconnected-(UPCH1F-GPP_A1/LAD0/ESPI_IO0-PadBB39)
- UPCH1 pad BB4: (no net) -> unconnected-(UPCH1M-CNV_WR_D0P-PadBB4)
- UPCH1 pad BB41: (no net) -> GND
- UPCH1 pad BB43: (no net) -> GND
- UPCH1 pad BB44: (no net) -> unconnected-(UPCH1A-INTRUDER#-PadBB44)
- UPCH1 pad BB46: (no net) -> unconnected-(UPCH1D-DRAM_RESET#-PadBB46)
- UPCH1 pad BB47: (no net) -> unconnected-(UPCH1D-WAKE#-PadBB47)
- UPCH1 pad BB6: (no net) -> unconnected-(UPCH1M-CNV_WT_CLKP-PadBB6)
- UPCH1 pad BB7: (no net) -> unconnected-(UPCH1H-VCCPRIM_3P3-PadBB7)
- UPCH1 pad BB9: (no net) -> GND
- UPCH1 pad BC1: (no net) -> unconnected-(UPCH1M-RSVD3-PadBC1)
- UPCH1 pad BC10: (no net) -> GND
- UPCH1 pad BC13: (no net) -> GND
- UPCH1 pad BC15: (no net) -> GND
- UPCH1 pad BC17: (no net) -> unconnected-(UPCH1A-GPP_D22/SPI1_IO3-PadBC17)
- UPCH1 pad BC19: (no net) -> GND
- UPCH1 pad BC22: (no net) -> unconnected-(UPCH1K-GPP_C17/I2C0_SCL-PadBC22)
- UPCH1 pad BC24: (no net) -> GND
- UPCH1 pad BC26: (no net) -> GND
- UPCH1 pad BC28: (no net) -> unconnected-(UPCH1D-GPP_B12/SLP_S0#-PadBC28)
- UPCH1 pad BC31: (no net) -> GND
- UPCH1 pad BC33: (no net) -> unconnected-(UPCH1A-GPP_B4/CPU_GP3-PadBC33)
- UPCH1 pad BC35: (no net) -> GND
- UPCH1 pad BC37: (no net) -> unconnected-(UPCH1D-GPP_A13/SUSWARN#/SUSPWRDNACK-PadBC37)
- UPCH1 pad BC40: (no net) -> GND
- UPCH1 pad BC42: (no net) -> unconnected-(UPCH1D-GPD10/SLP_S5#-PadBC42)
- UPCH1 pad BC45: (no net) -> GND
- UPCH1 pad BC49: (no net) -> unconnected-(UPCH1H-VCCRTC-PadBC49)
- UPCH1 pad BC5: (no net) -> unconnected-(UPCH1M-CNV_WT_CLKN-PadBC5)
- UPCH1 pad BC8: (no net) -> GND
- UPCH1 pad BD1: (no net) -> unconnected-(UPCH1M-GPPJ_RCOMP_1P8-PadBD1)
- UPCH1 pad BD11: (no net) -> unconnected-(UPCH1D-HDA_BCLK/I2S0_SCLK-PadBD11)
- UPCH1 pad BD12: (no net) -> unconnected-(UPCH1D-I2S1_SFRM/SNDW2_CLK-PadBD12)
- UPCH1 pad BD16: (no net) -> unconnected-(UPCH1D-GPP_D19/DMIC_CLK0/SNDW4_CLK-PadBD16)
- UPCH1 pad BD17: (no net) -> unconnected-(UPCH1A-GPP_D21/SPI1_IO2-PadBD17)
- UPCH1 pad BD20: (no net) -> unconnected-(UPCH1K-GPP_C20/UART2_RXD-PadBD20)
- UPCH1 pad BD21: (no net) -> unconnected-(UPCH1K-GPP_C15/UART1_CTS#/ISH_UART1_CTS#-PadBD21)
- UPCH1 pad BD29: (no net) -> unconnected-(UPCH1K-GPP_B17/GSPI0_MISO-PadBD29)
- UPCH1 pad BD30: (no net) -> unconnected-(UPCH1K-GPP_B21/GSPI1_MISO-PadBD30)
- UPCH1 pad BD33: (no net) -> unconnected-(UPCH1D-GPP_B23/SML1ALERT#/PCHHOT#-PadBD33)
- UPCH1 pad BD34: (no net) -> unconnected-(UPCH1K-GPP_A19/ISH_GP1-PadBD34)
- UPCH1 pad BD38: (no net) -> unconnected-(UPCH1K-GPP_A17/SD_VDD1_PWR_EN#/ISH_GP7-PadBD38)
- UPCH1 pad BD39: (no net) -> unconnected-(UPCH1D-SLP_SUS#-PadBD39)
- UPCH1 pad BD4: (no net) -> unconnected-(UPCH1M-CNV_WR_CLKN-PadBD4)
- UPCH1 pad BD42: (no net) -> unconnected-(UPCH1D-GPD9/SLP_WLAN#-PadBD42)
- UPCH1 pad BD43: (no net) -> GND
- UPCH1 pad BD46: (no net) -> unconnected-(UPCH1D-SRTCRST#-PadBD46)
- UPCH1 pad BD49: (no net) -> unconnected-(UPCH1H-VCCRTC-PadBD49)
- UPCH1 pad BD7: (no net) -> unconnected-(UPCH1M-CNV_WT_D0P-PadBD7)
- UPCH1 pad BD8: (no net) -> unconnected-(UPCH1M-GPP_G6/SD_CLK-PadBD8)
- UPCH1 pad BE1: (no net) -> unconnected-(UPCH1M-GPPJ_RCOMP_1P8-PadBE1)
- UPCH1 pad BE10: (no net) -> unconnected-(UPCH1D-HDA_RST#/I2S1_SCLK-PadBE10)
- UPCH1 pad BE11: (no net) -> unconnected-(UPCH1D-HDA_SDI0/I2S0_RXD-PadBE11)
- UPCH1 pad BE12: (no net) -> unconnected-(UPCH1D-I2S1_TXD/SNDW2_DATA-PadBE12)
- UPCH1 pad BE14: (no net) -> unconnected-(UPCH1K-GPP_D23/ISH_I2C2_SCL/I2C3_SCL-PadBE14)
- UPCH1 pad BE15: (no net) -> unconnected-(UPCH1K-GPP_D4/ISH_I2C2_SDA/I2C3_SDA/SBK4/BK4-PadBE15)
- UPCH1 pad BE16: (no net) -> unconnected-(UPCH1D-GPP_D5/I2S2_SFRM/CNV_RF_RESET#-PadBE16)
- UPCH1 pad BE17: (no net) -> unconnected-(UPCH1K-GPP_D13/ISH_UART0_RXD/I2C2_SDA-PadBE17)
- UPCH1 pad BE18: (no net) -> unconnected-(UPCH1A-GPP_D2/SPI1_MISO/SBK2/BK2-PadBE18)
- UPCH1 pad BE19: (no net) -> unconnected-(UPCH1A-GPP_D1/SPI1_CLK/SBK1/BK1-PadBE19)
- UPCH1 pad BE2: (no net) -> unconnected-(UPCH1M-GPPJ_RCOMP_1P8-PadBE2)
- UPCH1 pad BE20: (no net) -> unconnected-(UPCH1K-GPP_C21/UART2_TXD-PadBE20)
- UPCH1 pad BE21: (no net) -> unconnected-(UPCH1K-GPP_C19/I2C1_SCL-PadBE21)
- UPCH1 pad BE23: (no net) -> unconnected-(UPCH1K-GPP_C8/UART0_RXD-PadBE23)
- UPCH1 pad BE24: (no net) -> unconnected-(UPCH1D-GPP_C4/SML0DATA-PadBE24)
- UPCH1 pad BE25: (no net) -> unconnected-(UPCH1D-GPP_C2/SMBALERT#-PadBE25)
- UPCH1 pad BE26: (no net) -> unconnected-(UPCH1D-GPP_C0/SMBCLK-PadBE26)
- UPCH1 pad BE27: (no net) -> unconnected-(UPCH1D-GPP_C7/SML1DATA-PadBE27)
- UPCH1 pad BE29: (no net) -> unconnected-(UPCH1D-GPP_B0/GSPI0_CS1#-PadBE29)
- UPCH1 pad BE3: (no net) -> unconnected-(UPCH1M-CNV_WR_CLKP-PadBE3)
- UPCH1 pad BE30: (no net) -> unconnected-(UPCH1K-GPP_B18/GSPI0_MOSI-PadBE30)
- UPCH1 pad BE31: (no net) -> unconnected-(UPCH1G-GPP_B6/SRCCLKREQ1#-PadBE31)
- UPCH1 pad BE32: (no net) -> unconnected-(UPCH1D-GPP_B2/VRALERT#-PadBE32)
- UPCH1 pad BE33: (no net) -> unconnected-(UPCH1G-GPP_A16/CLKOUT_48-PadBE33)
- UPCH1 pad BE34: (no net) -> unconnected-(UPCH1K-GPP_A20/ISH_GP2-PadBE34)
- UPCH1 pad BE35: (no net) -> unconnected-(UPCH1D-GPP_A15/SUSACK#-PadBE35)
- UPCH1 pad BE36: (no net) -> unconnected-(UPCH1A-GPP_A11/PME#/SD_VDD2_PWR_EN#-PadBE36)
- UPCH1 pad BE38: (no net) -> unconnected-(UPCH1F-GPP_A5/LFRAME#/ESPI_CS0#-PadBE38)
- UPCH1 pad BE39: (no net) -> unconnected-(UPCH1F-GPP_A0/RCIN#/ESPI_ALERT1#-PadBE39)
- UPCH1 pad BE4: (no net) -> unconnected-(UPCH1M-SD_3P3_RCOMP-PadBE4)
- UPCH1 pad BE40: (no net) -> unconnected-(UPCH1D-GPD6/SLP_A#-PadBE40)
- UPCH1 pad BE41: (no net) -> unconnected-(UPCH1B-GPD7-PadBE41)
- UPCH1 pad BE42: (no net) -> unconnected-(UPCH1D-GPD5/SLP_S4#-PadBE42)
- UPCH1 pad BE44: (no net) -> GND
- UPCH1 pad BE45: (no net) -> unconnected-(UPCH1D-GPD8/SUSCLK-PadBE45)
- UPCH1 pad BE46: (no net) -> unconnected-(UPCH1D-GPD3/PWRBTN#-PadBE46)
- UPCH1 pad BE47: (no net) -> unconnected-(UPCH1D-RTCRST#-PadBE47)
- UPCH1 pad BE48: (no net) -> unconnected-(UPCH1H-VCCDSW_3P3-PadBE48)
- UPCH1 pad BE49: (no net) -> unconnected-(UPCH1H-VCCDSW_3P3-PadBE49)
- UPCH1 pad BE5: (no net) -> unconnected-(UPCH1M-SD_1P8_RCOMP-PadBE5)
- UPCH1 pad BE6: (no net) -> unconnected-(UPCH1M-CNV_WT_D0N-PadBE6)
- UPCH1 pad BE8: (no net) -> unconnected-(UPCH1M-GPP_G5/SD_CD#-PadBE8)
- UPCH1 pad BE9: (no net) -> unconnected-(UPCH1M-GPP_G1/SD_DATA0-PadBE9)
- UPCH1 pad BF1: (no net) -> GND
- UPCH1 pad BF10: (no net) -> unconnected-(UPCH1D-HDA_SDI1/I2S1_RXD-PadBF10)
- UPCH1 pad BF12: (no net) -> unconnected-(UPCH1D-HDA_SDO/I2S0_TXD-PadBF12)
- UPCH1 pad BF14: (no net) -> unconnected-(UPCH1K-GPP_D16/ISH_UART0_CTS#/CNV_WCEN-PadBF14)
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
